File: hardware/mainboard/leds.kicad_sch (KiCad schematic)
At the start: 8 parts

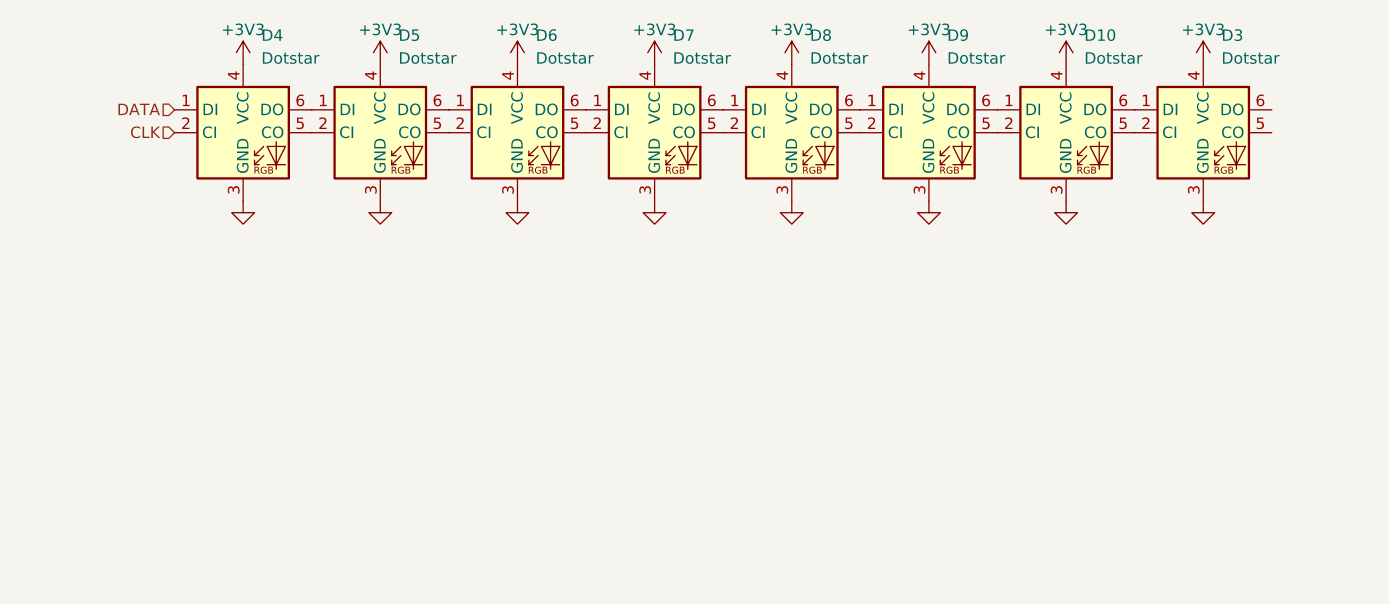
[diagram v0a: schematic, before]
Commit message: Progress on cleaning up the schematics
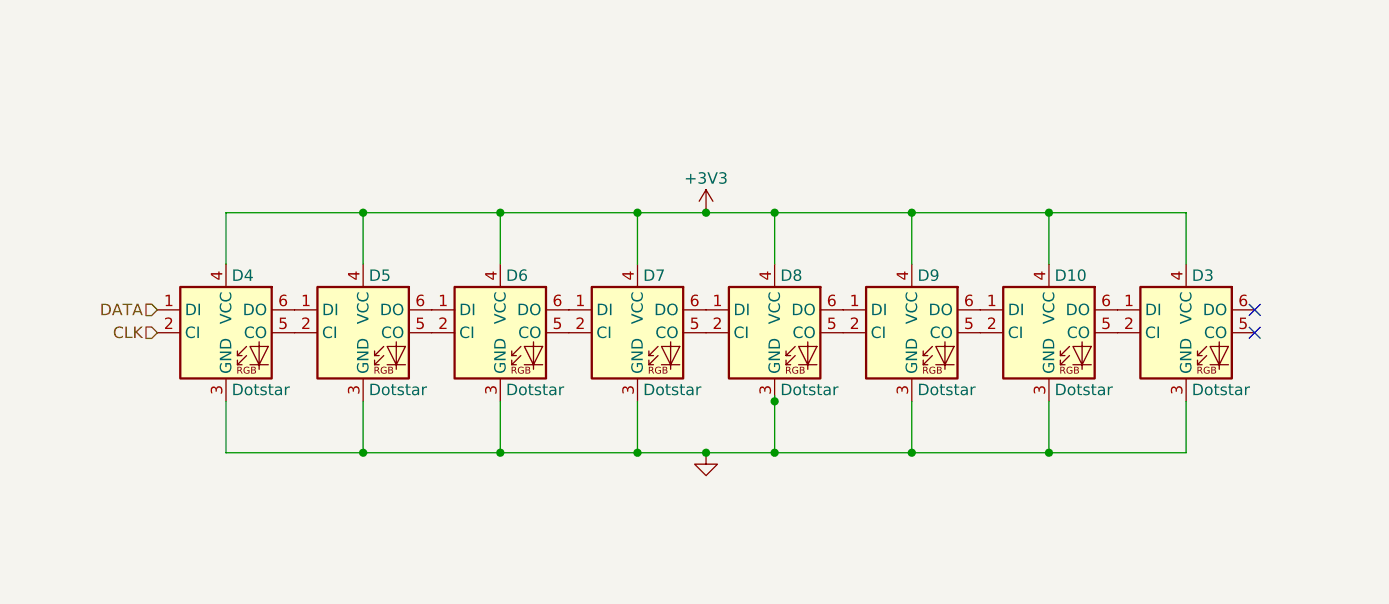
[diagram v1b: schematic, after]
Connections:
- no-connect marks 0 -> 2
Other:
- company: (none) -> Winterbloom
- title: (none) -> Castor & Pollux
- moved on the sheet: D10, D3, D4, D5, D6, D7, D8, D9

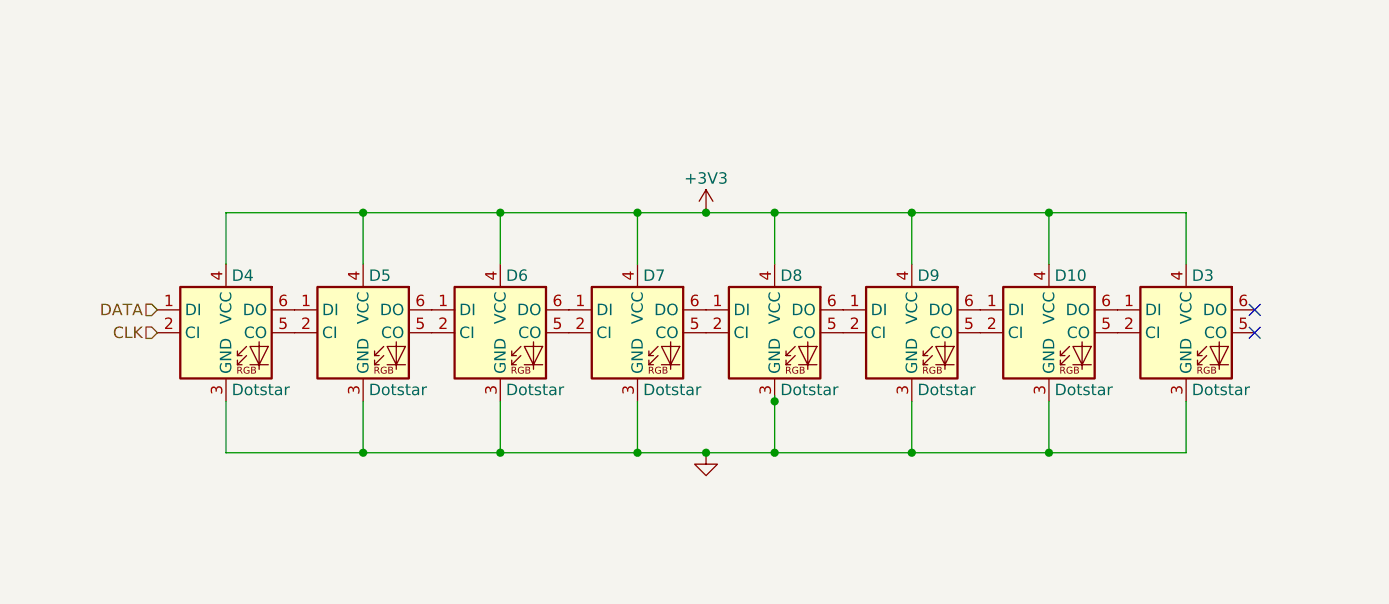
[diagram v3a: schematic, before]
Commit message: Reannotate schematic
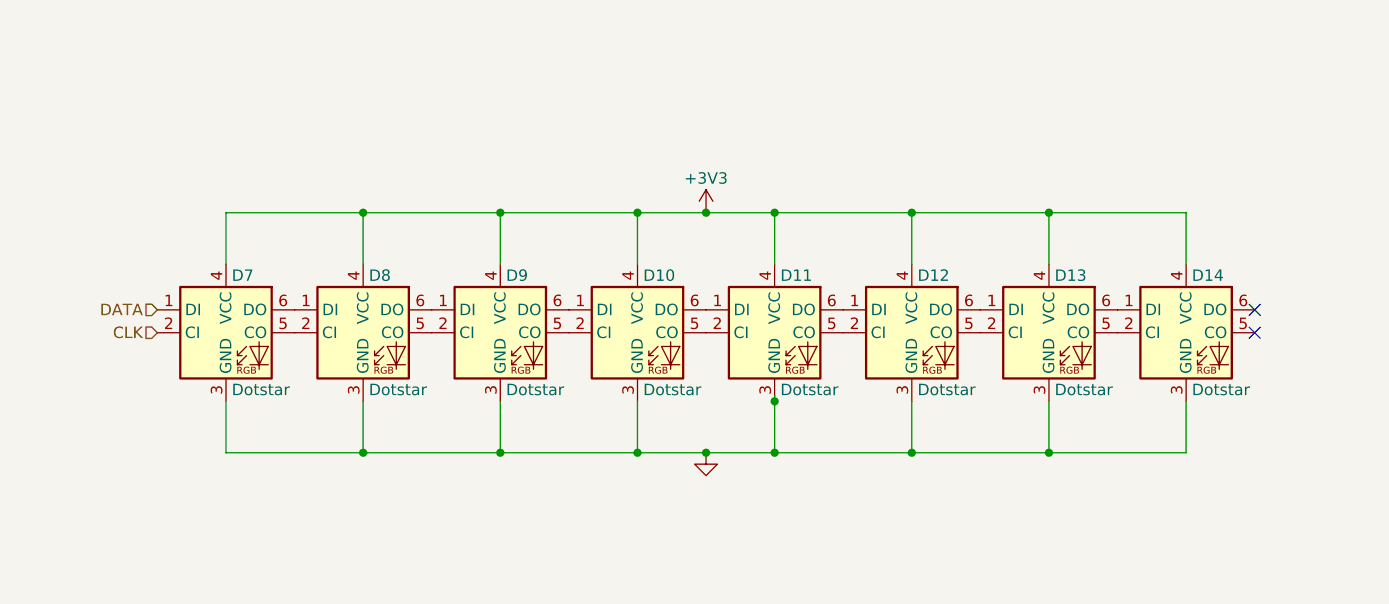
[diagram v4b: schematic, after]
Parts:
- renumbered D7 to D10, D8 to D11, D9 to D12, D10 to D13, D3 to D14, D4 to D7, D5 to D8, D6 to D9
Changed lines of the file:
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@@
   (symbol (lib_id "winterbloom:Dotstar") (at 182.88 99.06 0) (unit 1)
     (in_bom yes) (on_board yes)
-    (property "Reference" "D10" (id 0) (at 183.515 92.71 0)
+    (property "Reference" "D13" (id 0) (at 183.515 92.71 0)
       (effects (font (size 1.27 1.27)) (justify left))
     )
@@
   (symbol (lib_id "winterbloom:Dotstar") (at 167.64 99.06 0) (unit 1)
     (in_bom yes) (on_board yes)
-    (property "Reference" "D9" (id 0) (at 168.275 92.71 0)
+    (property "Reference" "D12" (id 0) (at 168.275 92.71 0)
       (effects (font (size 1.27 1.27)) (justify left))
     )
@@
   (symbol (lib_id "winterbloom:Dotstar") (at 91.44 99.06 0) (unit 1)
     (in_bom yes) (on_board yes)
-    (property "Reference" "D4" (id 0) (at 92.075 92.71 0)
+    (property "Reference" "D7" (id 0) (at 92.075 92.71 0)
       (effects (font (size 1.27 1.27)) (justify left))
     )
@@
   (symbol (lib_id "winterbloom:Dotstar") (at 152.4 99.06 0) (unit 1)
     (in_bom yes) (on_board yes)
-    (property "Reference" "D8" (id 0) (at 153.035 92.71 0)
+    (property "Reference" "D11" (id 0) (at 153.035 92.71 0)
       (effects (font (size 1.27 1.27)) (justify left))
     )
@@
   (symbol (lib_id "winterbloom:Dotstar") (at 137.16 99.06 0) (unit 1)
     (in_bom yes) (on_board yes)
-    (property "Reference" "D7" (id 0) (at 137.795 92.71 0)
+    (property "Reference" "D10" (id 0) (at 137.795 92.71 0)
       (effects (font (size 1.27 1.27)) (justify left))
     )
@@
   (symbol (lib_id "winterbloom:Dotstar") (at 198.12 99.06 0) (unit 1)
     (in_bom yes) (on_board yes)
-    (property "Reference" "D3" (id 0) (at 198.755 92.71 0)
+    (property "Reference" "D14" (id 0) (at 198.755 92.71 0)
       (effects (font (size 1.27 1.27)) (justify left))
     )
@@
   (symbol (lib_id "winterbloom:Dotstar") (at 121.92 99.06 0) (unit 1)
     (in_bom yes) (on_board yes)
-    (property "Reference" "D6" (id 0) (at 122.555 92.71 0)
+    (property "Reference" "D9" (id 0) (at 122.555 92.71 0)
       (effects (font (size 1.27 1.27)) (justify left))
     )
@@
   (symbol (lib_id "power:GND") (at 144.78 112.395 0) (unit 1)
     (in_bom yes) (on_board yes) (fields_autoplaced)
-    (property "Reference" "#PWR0162" (id 0) (at 144.78 118.745 0)
+    (property "Reference" "#PWR095" (id 0) (at 144.78 118.745 0)
       (effects (font (size 1.27 1.27)) hide)
     )
@@
   (symbol (lib_id "power:+3V3") (at 144.78 85.725 0) (unit 1)
     (in_bom yes) (on_board yes)
-    (property "Reference" "#PWR0159" (id 0) (at 144.78 89.535 0)
+    (property "Reference" "#PWR094" (id 0) (at 144.78 89.535 0)
       (effects (font (size 1.27 1.27)) hide)
     )
@@
   (symbol (lib_id "winterbloom:Dotstar") (at 106.68 99.06 0) (unit 1)
     (in_bom yes) (on_board yes)
-    (property "Reference" "D5" (id 0) (at 107.315 92.71 0)
-      (effects (font (size 1.27 1.27)) (justify left))
-    )
+    (property "Reference" "D8" (id 0) (at 107.315 92.71 0)
+      (effects (font (size 1.27 1.27)) (justify left))
+    )

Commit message: Audit BOM, replace some parts with alts
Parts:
- D10, D11, D12, D13, D14, D7, D8, D9: finalized (none) -> yes
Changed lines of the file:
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@@
+      (effects (font (size 1.27 1.27)) hide)
+    )
+    (property "finalized" "yes" (id 5) (at 182.88 99.06 0)
       (effects (font (size 1.27 1.27)) hide)
     )
@@
       (effects (font (size 1.27 1.27)) hide)
     )
+    (property "finalized" "yes" (id 5) (at 167.64 99.06 0)
+      (effects (font (size 1.27 1.27)) hide)
+    )
     (pin "1")
     (pin "2")
@@
       (effects (font (size 1.27 1.27)) hide)
     )
+    (property "finalized" "yes" (id 5) (at 91.44 99.06 0)
+      (effects (font (size 1.27 1.27)) hide)
+    )
     (pin "1")
     (pin "2")
@@
       (effects (font (size 1.27 1.27)) hide)
     )
+    (property "finalized" "yes" (id 5) (at 152.4 99.06 0)
+      (effects (font (size 1.27 1.27)) hide)
+    )
     (pin "1")
     (pin "2")
@@
       (effects (font (size 1.27 1.27)) hide)
     )
+    (property "finalized" "yes" (id 5) (at 137.16 99.06 0)
+      (effects (font (size 1.27 1.27)) hide)
+    )
     (pin "1")
     (pin "2")
@@
       (effects (font (size 1.27 1.27)) hide)
     )
+    (property "finalized" "yes" (id 5) (at 198.12 99.06 0)
+      (effects (font (size 1.27 1.27)) hide)
+    )
     (pin "1")
     (pin "2")
@@
     )
     (property "mpn" "SK9822" (id 4) (at 127 109.22 0)
+      (effects (font (size 1.27 1.27)) hide)
+    )
+    (property "finalized" "yes" (id 5) (at 121.92 99.06 0)
       (effects (font (size 1.27 1.27)) hide)
     )
@@
       (effects (font (size 1.27 1.27)) hide)
     )
+    (property "finalized" "yes" (id 5) (at 106.68 99.06 0)
+      (effects (font (size 1.27 1.27)) hide)
+    )

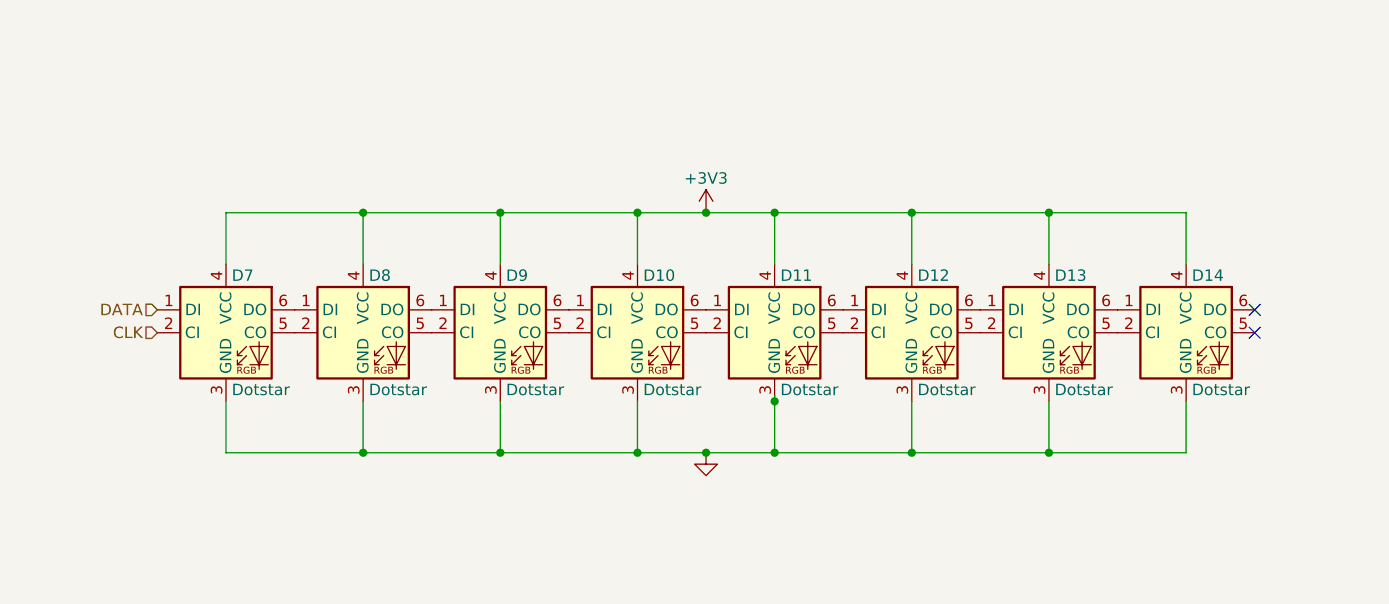
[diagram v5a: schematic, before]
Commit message: A little more schematic cleanup
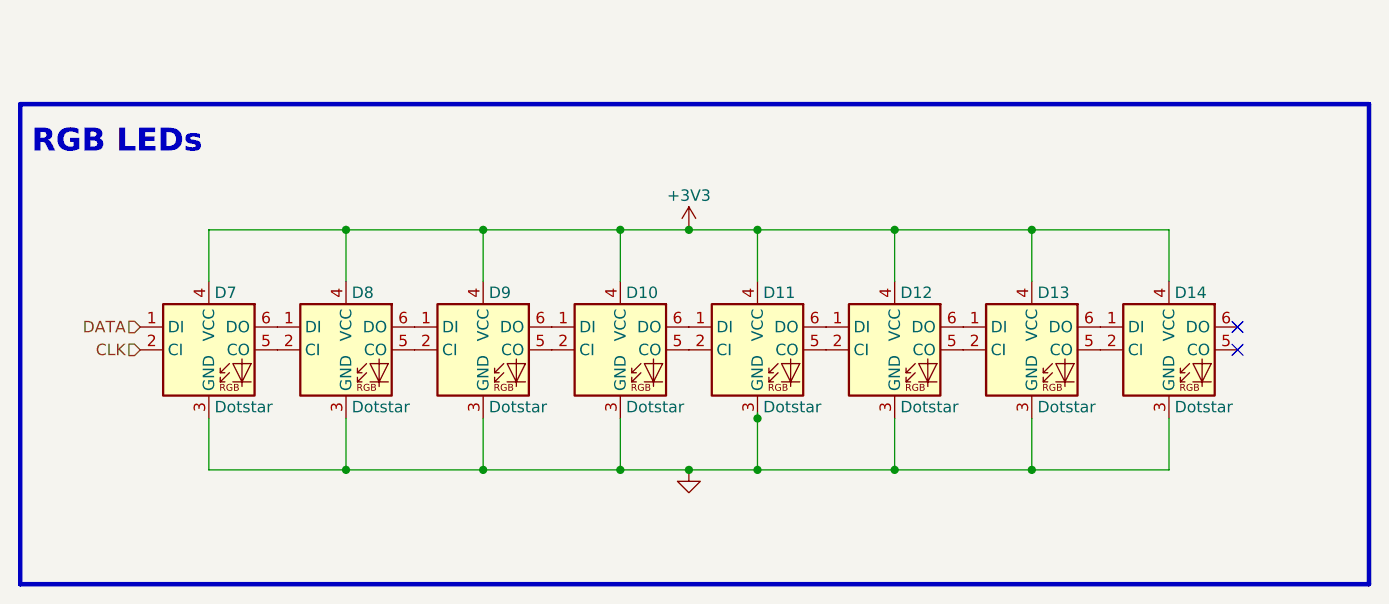
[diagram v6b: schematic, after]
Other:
- note added: "RGB LEDs"
- moved on the sheet: D10, D11, D12, D13, D14, D7, D8, D9

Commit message: hardware: fixup schematic fields
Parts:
- D10, D11, D12, D13, D14, D7, D8, D9: MPN (none) -> SK9822; finalized yes -> (none); mpn SK9822 -> (none)
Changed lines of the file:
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@@
       (effects (font (size 1.27 1.27)) (justify left top) hide)
     )
-    (property "mpn" "SK9822" (id 4) (at 186.055 111.125 0)
-      (effects (font (size 1.27 1.27)) hide)
-    )
-    (property "finalized" "yes" (id 5) (at 180.975 100.965 0)
+    (property "MPN" "SK9822" (id 4) (at 186.055 111.125 0)
       (effects (font (size 1.27 1.27)) hide)
     )
@@
       (effects (font (size 1.27 1.27)) (justify left top) hide)
     )
-    (property "mpn" "SK9822" (id 4) (at 170.815 111.125 0)
-      (effects (font (size 1.27 1.27)) hide)
-    )
-    (property "finalized" "yes" (id 5) (at 165.735 100.965 0)
+    (property "MPN" "SK9822" (id 4) (at 170.815 111.125 0)
       (effects (font (size 1.27 1.27)) hide)
     )
@@
       (effects (font (size 1.27 1.27)) (justify left top) hide)
     )
-    (property "mpn" "SK9822" (id 4) (at 94.615 111.125 0)
-      (effects (font (size 1.27 1.27)) hide)
-    )
-    (property "finalized" "yes" (id 5) (at 89.535 100.965 0)
+    (property "MPN" "SK9822" (id 4) (at 94.615 111.125 0)
       (effects (font (size 1.27 1.27)) hide)
     )
@@
       (effects (font (size 1.27 1.27)) (justify left top) hide)
     )
-    (property "mpn" "SK9822" (id 4) (at 155.575 111.125 0)
-      (effects (font (size 1.27 1.27)) hide)
-    )
-    (property "finalized" "yes" (id 5) (at 150.495 100.965 0)
+    (property "MPN" "SK9822" (id 4) (at 155.575 111.125 0)
       (effects (font (size 1.27 1.27)) hide)
     )
@@
       (effects (font (size 1.27 1.27)) (justify left top) hide)
     )
-    (property "mpn" "SK9822" (id 4) (at 140.335 111.125 0)
-      (effects (font (size 1.27 1.27)) hide)
-    )
-    (property "finalized" "yes" (id 5) (at 135.255 100.965 0)
+    (property "MPN" "SK9822" (id 4) (at 140.335 111.125 0)
       (effects (font (size 1.27 1.27)) hide)
     )
@@
       (effects (font (size 1.27 1.27)) (justify left top) hide)
     )
-    (property "mpn" "SK9822" (id 4) (at 201.295 111.125 0)
-      (effects (font (size 1.27 1.27)) hide)
-    )
-    (property "finalized" "yes" (id 5) (at 196.215 100.965 0)
+    (property "MPN" "SK9822" (id 4) (at 201.295 111.125 0)
       (effects (font (size 1.27 1.27)) hide)
     )
@@
       (effects (font (size 1.27 1.27)) (justify left top) hide)
     )
-    (property "mpn" "SK9822" (id 4) (at 125.095 111.125 0)
-      (effects (font (size 1.27 1.27)) hide)
-    )
-    (property "finalized" "yes" (id 5) (at 120.015 100.965 0)
+    (property "MPN" "SK9822" (id 4) (at 125.095 111.125 0)
       (effects (font (size 1.27 1.27)) hide)
     )
@@
       (effects (font (size 1.27 1.27)) (justify left top) hide)
     )
-    (property "mpn" "SK9822" (id 4) (at 109.855 111.125 0)
-      (effects (font (size 1.27 1.27)) hide)
-    )
-    (property "finalized" "yes" (id 5) (at 104.775 100.965 0)
-      (effects (font (size 1.27 1.27)) hide)
-    )
+    (property "MPN" "SK9822" (id 4) (at 109.855 111.125 0)
+      (effects (font (size 1.27 1.27)) hide)
+    )
